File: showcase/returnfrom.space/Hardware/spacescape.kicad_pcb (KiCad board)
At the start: 2 copper layers, 224 x 112 mm, 88 parts, among them J1 USB_C_Receptacle_USB2.0_16P, J2 Conn_01x08_Socket, J20 Conn_01x08_Socket, J21 Conn_01x08_Socket, J22 USB_C_Receptacle_USB2.0_16P, J3 OLED, J4 Conn_02x04_Counter_Clockwise, J5 Conn_01x03_Pin, J6 Conn_01x05_Pin, J7 OLED, Q1 NPN, SW0 SW_SPST, SW1 SW_SPST, SW10 SW_SPST, SW11 SW_SPST, SW12 SW_SPST, SW13 SW_SPST, SW14 SW_SPST, SW15 SW_SPST, SW16 SW_SPST, SW17 RESET, SW18 BOOTSEL, SW2 SW_SPST, SW3 SW_SPST, SW4 SW_SPST, SW5 SW_SPST, SW6 SW_SPST, SW7 SW_SPST, SW8 SW_SPST, SW9 SW_SPST, U1 ATtiny1616-M, U2 ESP32-S2-SOLO, U3 RP2040, U4 MT3608, U5 LM324, U6 ESP32-S2-SOLO, U7 LIS2DH, U8 W25Q128JVS

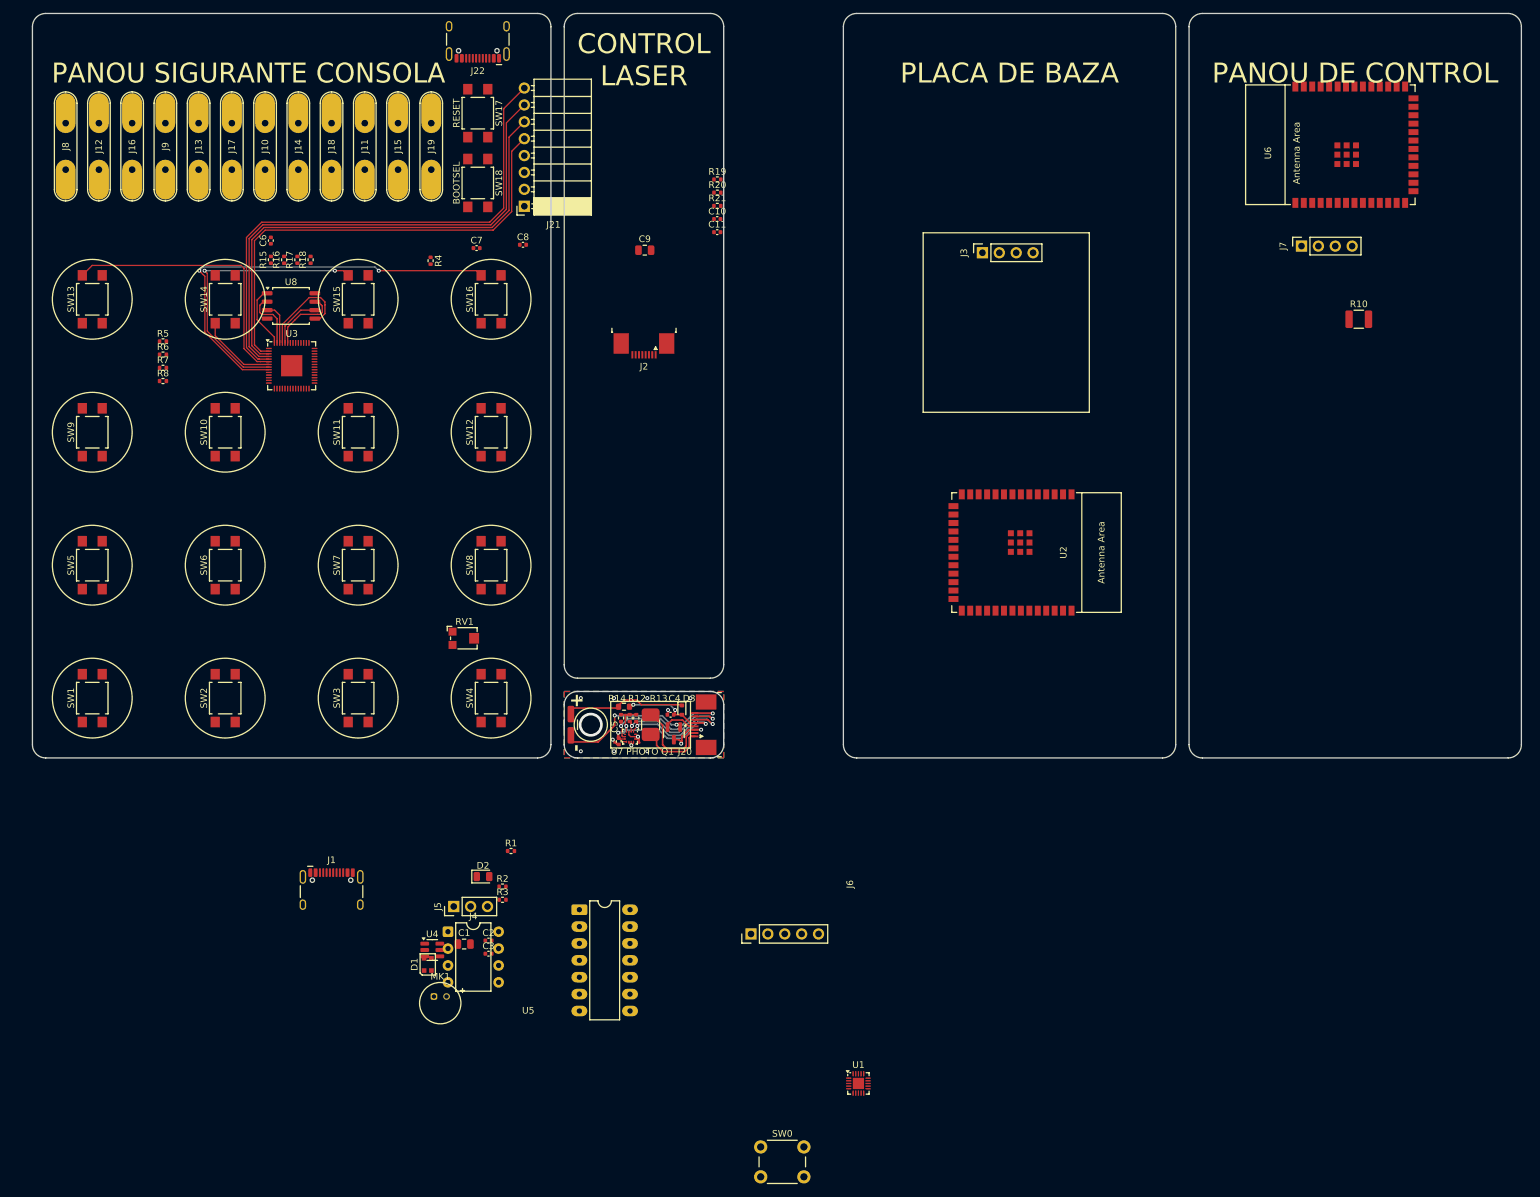
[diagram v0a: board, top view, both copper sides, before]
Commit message: added step files
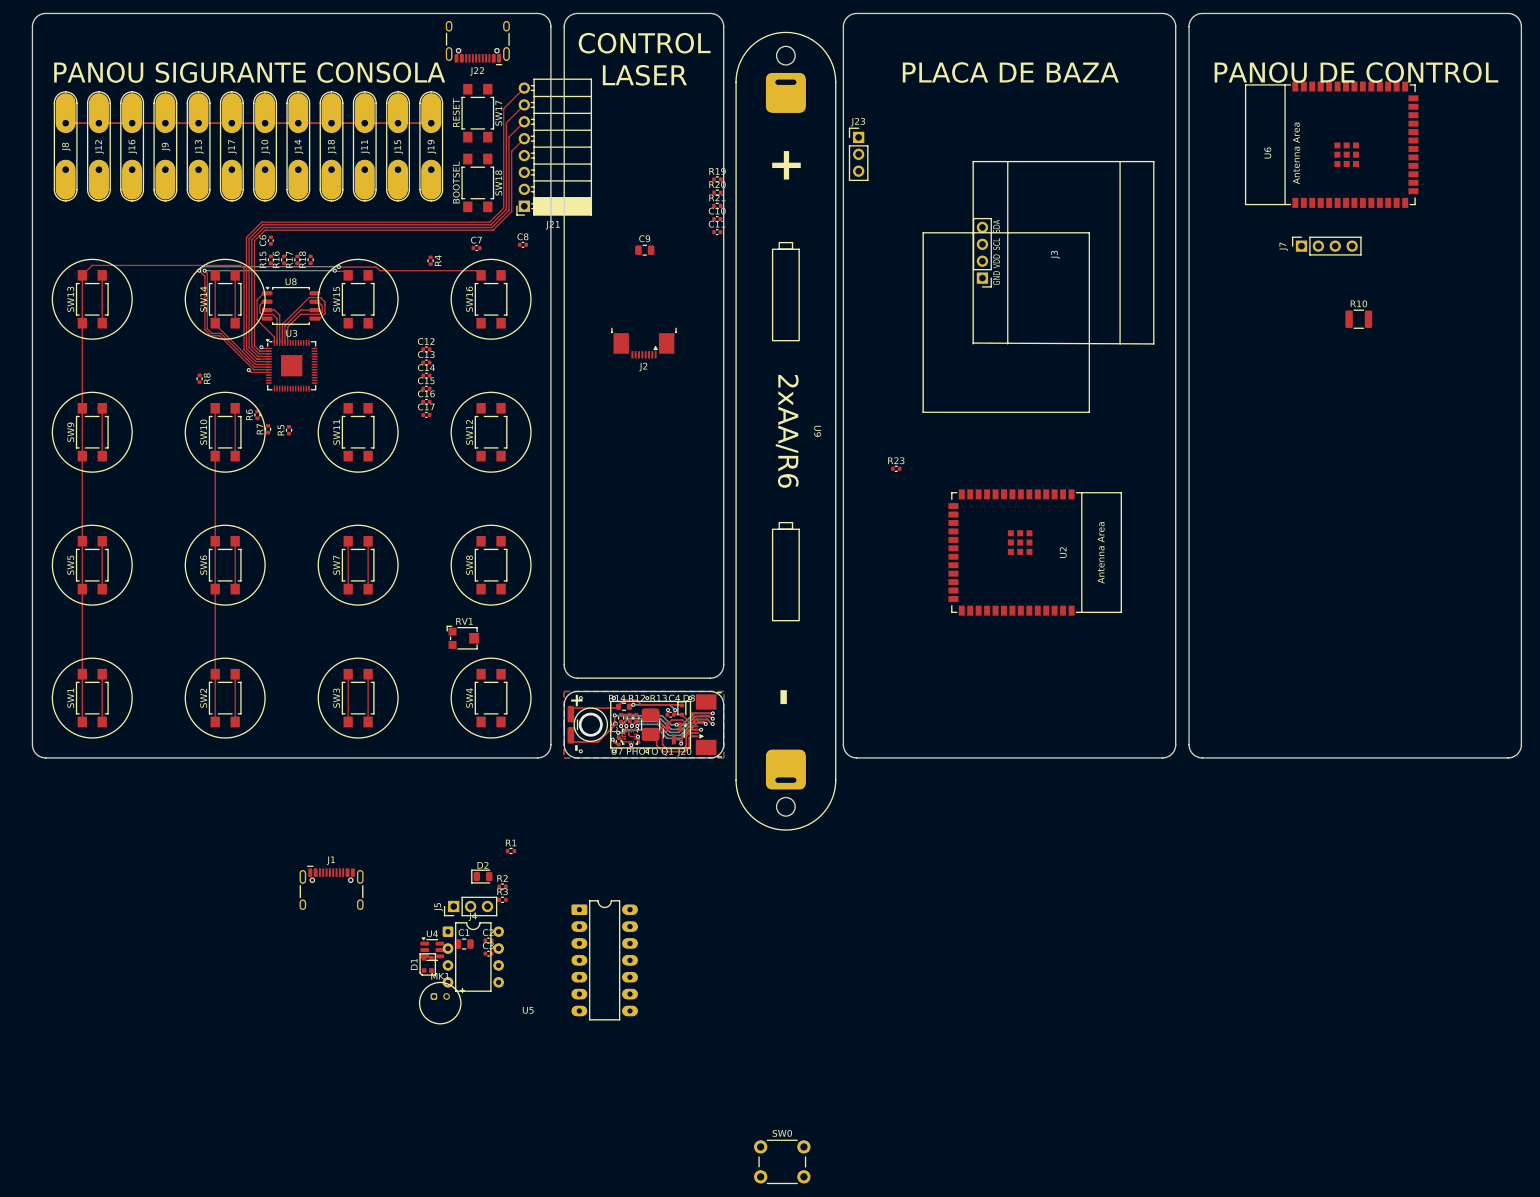
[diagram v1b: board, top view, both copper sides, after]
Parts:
- removed J6: Conn_01x05_Pin, Connector_PinHeader_2.54mm:PinHeader_1x05_P2.54mm_Vertical
- removed U1: ATtiny1616-M, Package_DFN_QFN:VQFN-20-1EP_3x3mm_P0.4mm_EP1.7x1.7mm
- added C12: 100nF, Capacitor_SMD:C_0402_1005Metric, F.Cu at (89.3, 80.5)
- added C13: 100nF, Capacitor_SMD:C_0402_1005Metric, F.Cu at (89.3, 82.5)
- added C14: 100nF, Capacitor_SMD:C_0402_1005Metric, F.Cu at (89.3, 84.5)
- added C15: 100nF, Capacitor_SMD:C_0402_1005Metric, F.Cu at (89.3, 86.5)
- added C16: 100nF, Capacitor_SMD:C_0402_1005Metric, F.Cu at (89.3, 88.4)
- added C17: 100nF, Capacitor_SMD:C_0402_1005Metric, F.Cu at (89.3, 90.4)
- added J23: Conn_01x03_Pin, Connector_PinHeader_2.54mm:PinHeader_1x03_P2.54mm_Vertical, F.Cu at (154.3, 48.6)
- added R23: 5K1, Resistor_SMD:R_0402_1005Metric, F.Cu at (159.9, 98.5)
- added U9: ~, spacescape:2xAA, F.Cu at (143.3, 92.8)
- J3: footprint Connector_PinSocket_2.54mm:PinSocket_1x04_P2.54mm_Vertical -> TG9541:Display_128x64_096_I2C
- moved R5 23.2 mm to (68.6, 92.7), turned to 90 degrees
- moved R7 18.3 mm to (65.5, 92.5), turned to 90 degrees
- moved R6 16.9 mm to (63.9, 90.4), turned to 90 degrees
- moved R8 5.52 mm to (55.1, 85.0), turned to -90 degrees
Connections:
- U3 pad 43: unconnected-(U3-ADC_AVDD-Pad43) -> Net-(U3-ADC_AVDD)
- U3 pad 44: unconnected-(U3-VREG_IN-Pad44) -> Net-(U3-VREG_IN)
- U3 pad 45: unconnected-(U3-VREG_VOUT-Pad45) -> Net-(U3-VREG_VOUT)
- U3 pad 48: unconnected-(U3-USB_VDD-Pad48) -> Net-(U3-USB_VDD)
- U4 pad 5: unconnected-(U4-IN-Pad5) -> Net-(J23-Pin_1)
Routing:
- net Net-(SW1-A): track 41.8 -> 109.1 mm
- net Net-(U3-GPIO26_ADC0): track 0.00 -> 55.0 mm
- net Net-(SW10-A): track 11.7 -> 65.1 mm
- net Net-(SW5-B): track 0.00 -> 21.6 mm
- net Net-(SW1-B): track 0.00 -> 21.6 mm
- net Net-(SW13-B): track 0.00 -> 14.4 mm
- net Net-(SW10-B): track 0.00 -> 14.4 mm
- net Net-(SW11-A): track 42.6 -> 56.8 mm
- net Net-(C17-Pad1): track 0.00 -> 4.35 mm, vias 0 -> 2
